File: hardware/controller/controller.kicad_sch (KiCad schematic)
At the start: 8 parts, among them SW1 RESET, U1 4050, U2 Pico, U3 Display_3.5", U4 4050, U5 Pico, U6 Display_3.5"

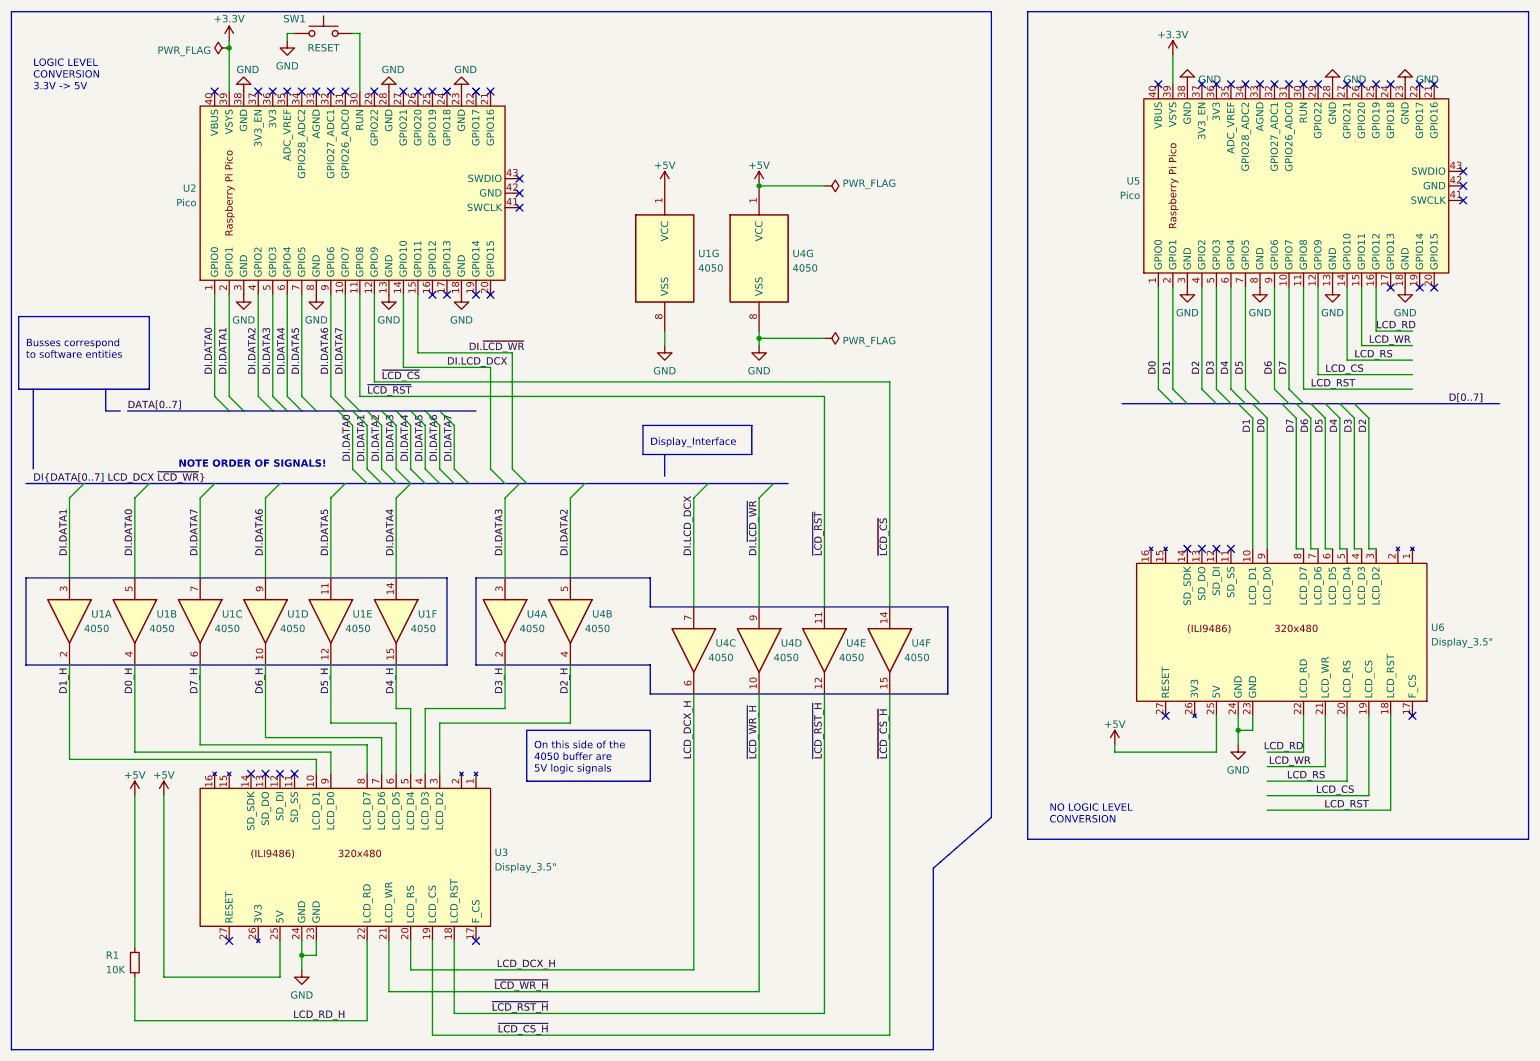
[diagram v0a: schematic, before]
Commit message: Removed 3.5 inch display from schematic
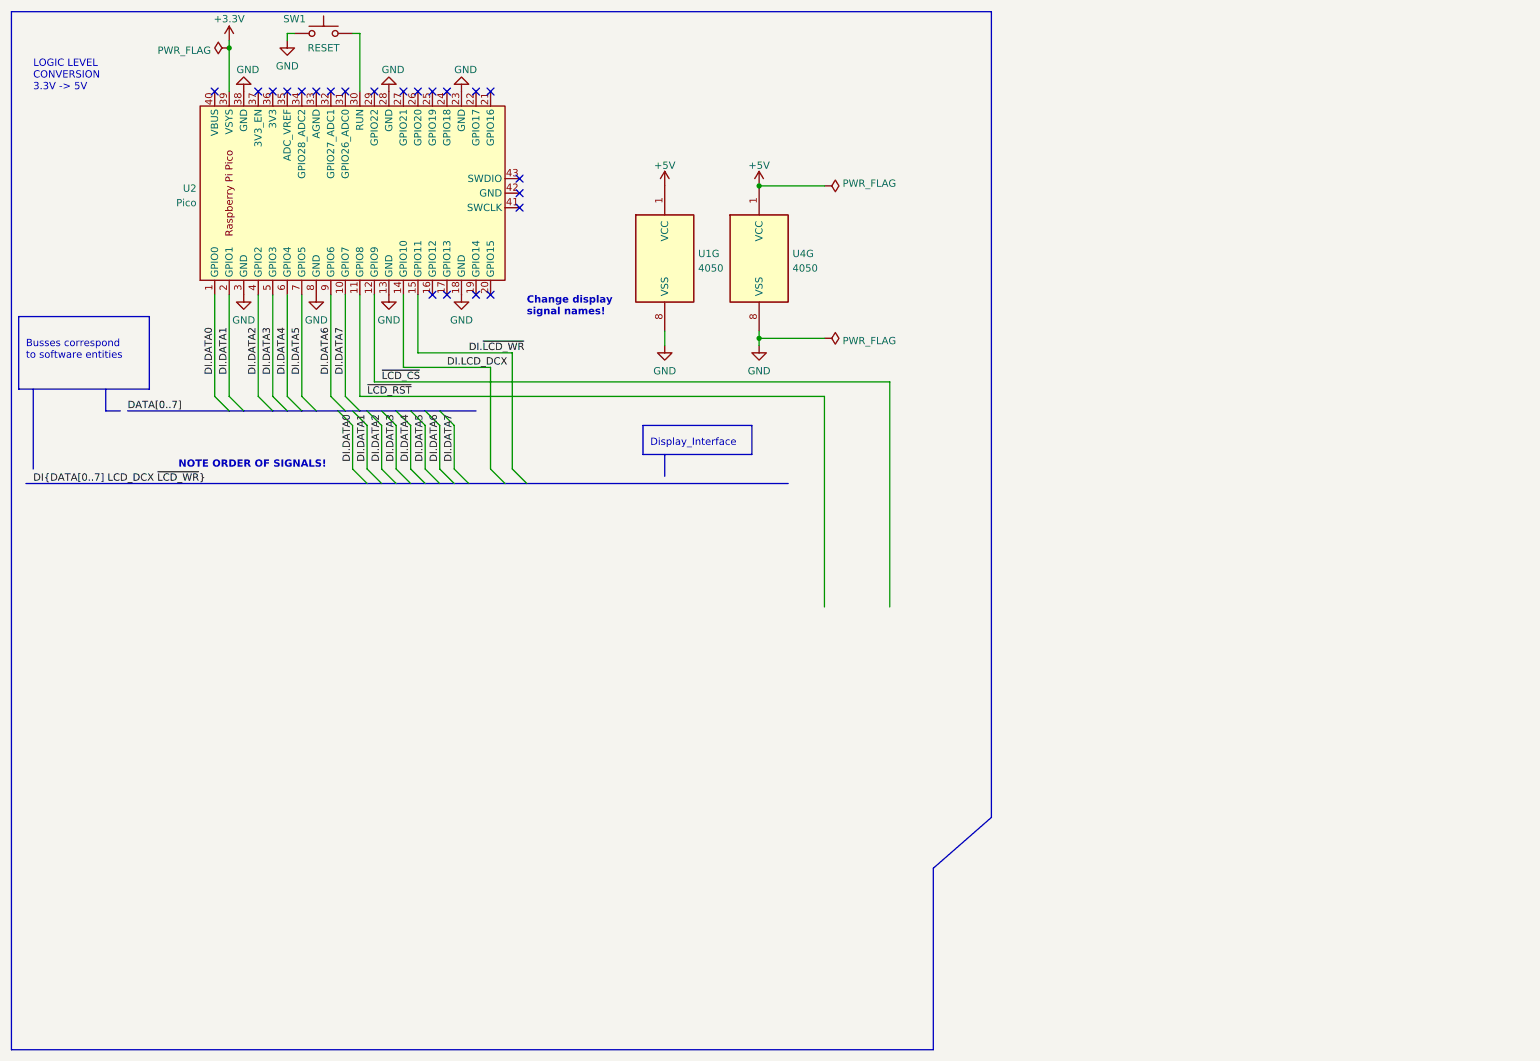
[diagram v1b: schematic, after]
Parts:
- removed R1: 10K, symbol Device:R_Small
- removed unit 1 of U1
- removed unit 2 of U1
- removed unit 3 of U1
- removed unit 5 of U1
- removed unit 4 of U1
- removed unit 6 of U1
- removed U3, U6: Display_3.5", symbol project:Display_3.5{dblquote}
- removed unit 4 of U4
- removed unit 1 of U4
- removed unit 6 of U4
- removed unit 3 of U4
- removed unit 5 of U4
- removed unit 2 of U4
- removed U5: Pico, RPi_Pico:RPi_Pico_SMD_TH, symbol MCU_RaspberryPi_and_Boards:Pico
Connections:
- no-connect marks 56 -> 22
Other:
- note added: "Change display signal names!"
- note removed: "NO LOGIC LEVEL CONVERSION"
- note removed: "On this side of the 4050 buffer are 5V logic signals"

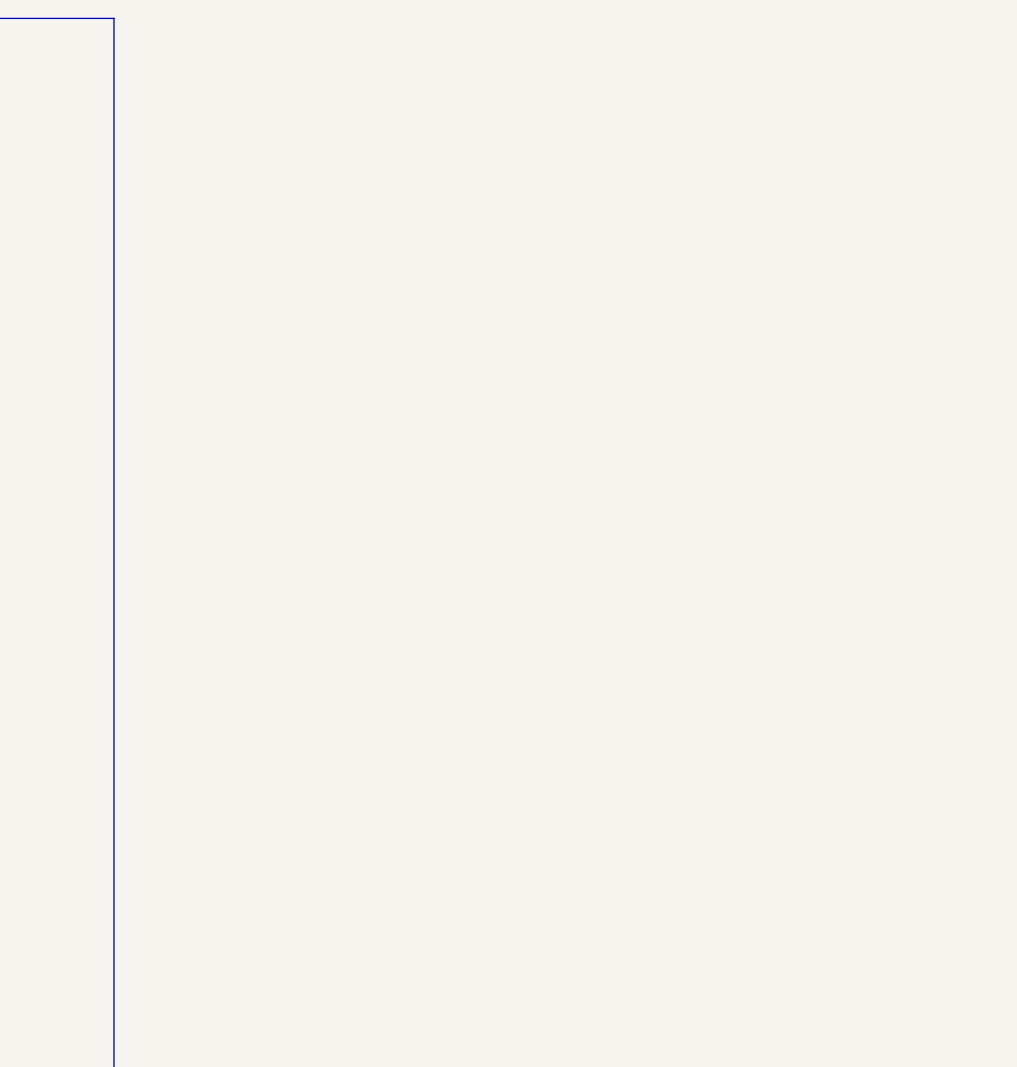
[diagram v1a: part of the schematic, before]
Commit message: Revised powerchain (diode, new symbol)
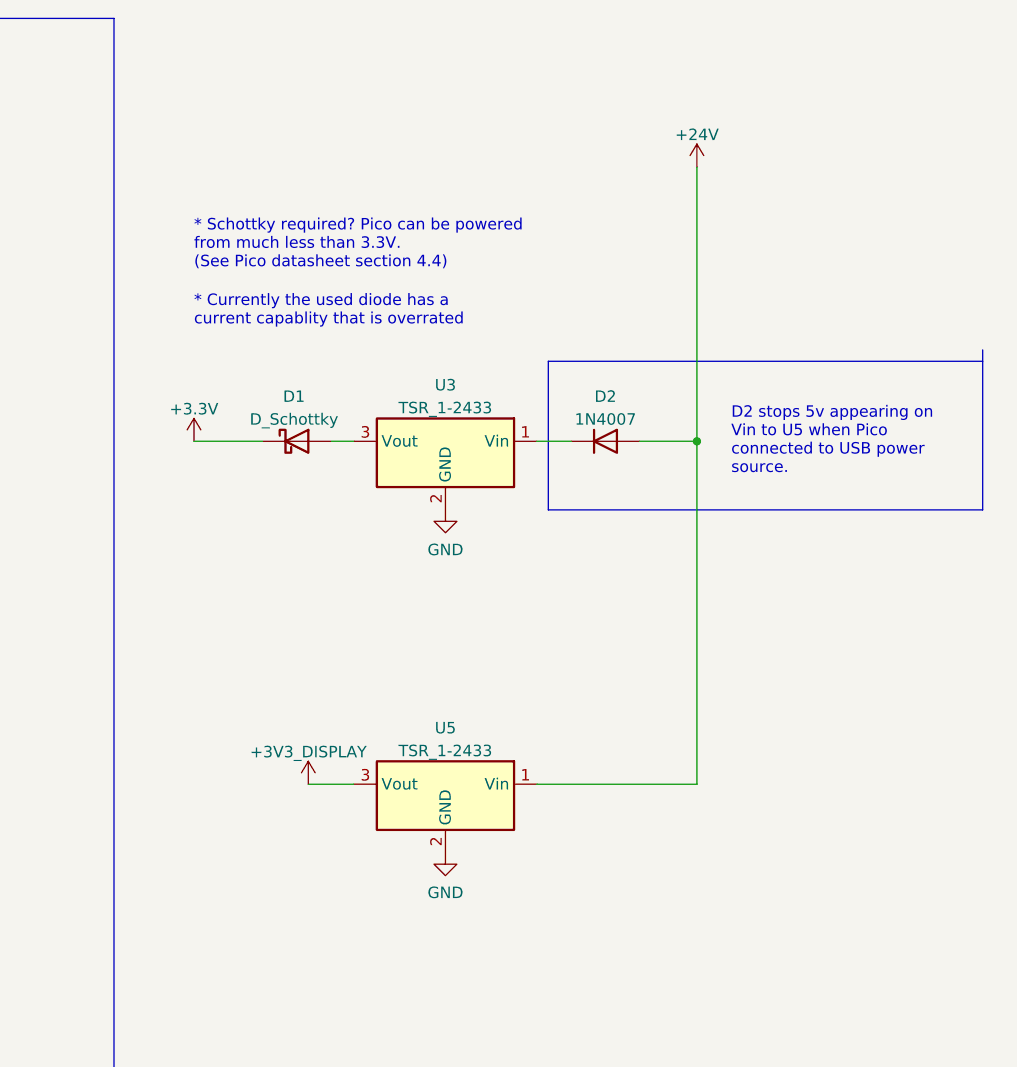
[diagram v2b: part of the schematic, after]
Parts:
- added D1: D_Schottky, symbol Device:D_Schottky
- added D2: 1N4007, Diode_THT:D_DO-41_SOD81_P10.16mm_Horizontal, symbol Diode:1N4007
- added U3, U5: TSR_1-2433, Converter_DCDC:Converter_DCDC_TRACO_TSR-1_THT, symbol Regulator_Switching:TSR_1-2433
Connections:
- net +3V3: now also D1.1 (K), U5.3 (Vout)
- net GND: now also U3.2 (GND), U5.2 (GND)
- new net: D2.1 (K), U3.1 (Vin)
- new net: D1.2 (A), U3.3 (Vout)
- new net +24V: D2.2 (A), U5.1 (Vin)
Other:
- note added: "* Currently the used diode has a current capablity that is overrated"
- note added: "* Schottky required? Pico can be powered from much less than 3.3V. (See Pico datasheet section 4.4)"
- note added: "D2 stops 5v appearing on Vin to U5 when Pico connected to USB power source."

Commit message: Added sense signal
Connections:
- net +3V3: now also U2.21 (GPIO16)
- no-connect marks 22 -> 21
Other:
- note added: "To GPIO16"
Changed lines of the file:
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@@
     (title "Modular-Amplifier - Controller")
+  )
+  (junction (at 209.55 100.33) (diameter 0) (color 0 0 0 0)
   )
   (junction (at 144.78 45.72) (diameter 0) (color 0 0 0 0)
@@
   (no_connect (at 95.25 64.77))
   (no_connect (at 97.79 64.77))
-  (no_connect (at 97.79 29.21))
   (no_connect (at 95.25 29.21))
   (no_connect (at 90.17 29.21))
@@
     (stroke (width 0) (type default) (color 0 0 0 0))
   )
+  (wire (pts (xy 209.55 100.33) (xy 212.09 100.33))
+    (stroke (width 0) (type default) (color 0 0 0 0))
+  )
   (bus (pts (xy 78.74 97.79) (xy 81.28 97.79))
     (stroke (width 0) (type default) (color 0 0 0 0))
@@
     (stroke (width 0) (type default) (color 0 0 0 0))
   )
+  (wire (pts (xy 195.58 106.68) (xy 209.55 106.68))
+    (stroke (width 0) (type default) (color 0 0 0 0))
+  )
+  (wire (pts (xy 97.79 29.21) (xy 97.79 21.59))
+    (stroke (width 0) (type default) (color 0 0 0 0))
+  )
   (polyline (pts (xy 124.46 87.63) (xy 124.46 92.71))
     (stroke (width 0) (type default) (color 0 0 0 0))
@@
     (stroke (width 0) (type default) (color 0 0 0 0))
   )
-  (polyline (pts (xy 281.94 52.07) (xy 281.94 69.85))
-    (stroke (width 0) (type default) (color 0 0 0 0))
-  )
   (wire (pts (xy 74.93 64.77) (xy 74.93 82.55))
     (stroke (width 0) (type default) (color 0 0 0 0))
@@
     (stroke (width 0) (type default) (color 0 0 0 0))
   )
+  (wire (pts (xy 97.79 21.59) (xy 111.76 21.59))
+    (stroke (width 0) (type default) (color 0 0 0 0))
+  )
   (wire (pts (xy 97.79 77.47) (xy 97.79 95.25))
     (stroke (width 0) (type default) (color 0 0 0 0))
@@
     (stroke (width 0) (type default) (color 0 0 0 0))
   )
-  (wire (pts (xy 207.01 100.33) (xy 212.09 100.33))
+  (wire (pts (xy 207.01 100.33) (xy 209.55 100.33))
     (stroke (width 0) (type default) (color 0 0 0 0))
   )
@@
   )
   (bus (pts (xy 81.28 85.09) (xy 83.82 85.09))
+    (stroke (width 0) (type default) (color 0 0 0 0))
+  )
+  (wire (pts (xy 209.55 100.33) (xy 209.55 106.68))
+    (stroke (width 0) (type default) (color 0 0 0 0))
+  )
+  (polyline (pts (xy 281.94 53.34) (xy 281.94 69.85))
     (stroke (width 0) (type default) (color 0 0 0 0))
   )
@@
     (effects (font (size 1.27 1.27) (thickness 0.254) bold) (justify left bottom))
   )
+  (text "To GPIO16" (at 196.85 110.49 0)
+    (effects (font (size 1.27 1.27)) (justify left bottom))
+  )
   (label "DI.DATA3" (at 59.69 78.74 90)
     (effects (font (size 1.27 1.27)) (justify left bottom))
@@
     (effects (font (size 1.27 1.27)) (justify left bottom))
   )
+  (label "SENSE" (at 104.14 21.59 0)
+    (effects (font (size 1.27 1.27)) (justify left bottom))
+  )
   (label "DI.DATA7" (at 72.39 78.74 90)
     (effects (font (size 1.27 1.27)) (justify left bottom))
@@
     (effects (font (size 1.27 1.27)) (justify left bottom))
   )
+  (label "SENSE" (at 196.85 106.68 0)
+    (effects (font (size 1.27 1.27)) (justify left bottom))
+  )

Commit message: Controller schematic and PCB design
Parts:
- removed U1, U4: 4050, symbol 4xxx:4050
- added H1, H2, H3, H4: MountingHole, MountingHole:MountingHole_3.2mm_M3, symbol Mechanical:MountingHole
- added J1: Conn_02x15_Odd_Even, Connector_PinSocket_2.54mm:PinSocket_2x15_P2.54mm_Vertical, symbol Connector_Generic:Conn_02x15_Odd_Even
- added J10: conn_wifi, Connector_JST:JST_PH_B8B-PH-K_1x08_P2.00mm_Vertical, symbol Connector_Generic:Conn_01x08
- added J11: conn_gpio, Connector_PinHeader_2.54mm:PinHeader_1x04_P2.54mm_Vertical, symbol Connector_Generic:Conn_01x04
- added J2, J3: Conn_01x20, Connector_PinSocket_2.54mm:PinSocket_1x20_P2.54mm_Vertical, symbol Connector_Generic:Conn_01x20
- added J4: Conn_01x02, Connector_JST:JST_XH_B2B-XH-A_1x02_P2.50mm_Vertical, symbol Connector_Generic:Conn_01x02
- added J5: conn_vol, Connector_JST:JST_PH_B5B-PH-K_1x05_P2.00mm_Vertical, symbol Connector_Generic:Conn_01x05
- added J6: conn_bl, Connector_JST:JST_PH_B5B-PH-K_1x05_P2.00mm_Vertical, symbol Connector_Generic:Conn_01x05
- added J7: conn_br, Connector_JST:JST_PH_B5B-PH-K_1x05_P2.00mm_Vertical, symbol Connector_Generic:Conn_01x05
- added J8: conn_dsp, Connector_JST:JST_PH_B4B-PH-K_1x04_P2.00mm_Vertical, symbol Connector_Generic:Conn_01x04
- added J9: conn_i2s_mplx, Connector_JST:JST_PH_B4B-PH-K_1x04_P2.00mm_Vertical, symbol Connector_Generic:Conn_01x04
- added R1: 10k, Resistor_SMD:R_0805_2012Metric_Pad1.20x1.40mm_HandSolder, symbol Device:R_Small
- added R2, R3: 2.2K, Resistor_SMD:R_0805_2012Metric_Pad1.20x1.40mm_HandSolder, symbol Device:R_Small
- added U1: Display_5"_RA8875, symbol project:Display_5{dblquote}_RA8875
- added U2: TSR_1-2433, Converter_DCDC:Converter_DCDC_TRACO_TSR-1_THT, symbol Regulator_Switching:TSR_1-2433
- D1: footprint (none) -> Diode_THT:D_DO-15_P12.70mm_Horizontal; Source (none) -> https://www.conrad.de/de/p/tru-components-schottky-diode-gl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; Uf (none) -> 500mV
- SW1: footprint (none) -> Button_Switch_THT:SW_PUSH_6mm_H4.3mm
- renumbered U2 to #U2
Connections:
- net +24V: now also J4.1 (Pin_1), U2.1 (Vin)
- net +3V3: now also J11.2 (Pin_2), J3.19 (Pin_19), J5.4 (Pin_4), J6.2 (Pin_2), J7.2 (Pin_2), J9.2 (Pin_2), R2.1, R3.1; no longer #U2.21 (GPIO16), U5.3 (Vout)
- net DI.DATA0: now also #U2.17 (GPIO13), J1.15 (Pin_15), J2.17 (Pin_17), U1.15 (DB0); no longer #U2.1 (GPIO0)
- net DI.DATA1: now also #U2.16 (GPIO12), J1.16 (Pin_16), J2.16 (Pin_16), U1.16 (DB1); no longer #U2.2 (GPIO1)
- net DI.DATA2: now also #U2.15 (GPIO11), J1.17 (Pin_17), J2.15 (Pin_15), U1.17 (DB2); no longer #U2.4 (GPIO2)
- net DI.DATA3: now also #U2.14 (GPIO10), J1.18 (Pin_18), J2.14 (Pin_14), U1.18 (DB3); no longer #U2.5 (GPIO3)
- net DI.DATA4: now also J1.19 (Pin_19), J3.6 (Pin_6), U1.19 (DB4); no longer #U2.6 (GPIO4)
- net DI.DATA5: now also #U2.27 (GPIO21), J1.20 (Pin_20), J3.7 (Pin_7), U1.20 (DB5); no longer #U2.7 (GPIO5)
- net DI.DATA6: now also #U2.29 (GPIO22), J1.21 (Pin_21), J3.9 (Pin_9), U1.21 (DB6); no longer #U2.9 (GPIO6)
- net DI.DATA7: now also #U2.31 (GPIO26_ADC0), J1.22 (Pin_22), J3.11 (Pin_11), U1.22 (DB7); no longer #U2.10 (GPIO7)
- net DI.LCD_DCX: now also #U2.32 (GPIO27_ADC1), J1.8 (Pin_8), J3.12 (Pin_12), U1.8 (RS); no longer #U2.14 (GPIO10)
- net DI.~{LCD_WR}: now also #U2.34 (GPIO28_ADC2), J1.6 (Pin_6), J3.14 (Pin_14), U1.6 (WR); no longer #U2.15 (GPIO11)
- net GND: now also J1.1 (Pin_1), J1.13 (Pin_13), J1.2 (Pin_2), J10.1 (Pin_1), J11.1 (Pin_1), J2.13 (Pin_13), J2.18 (Pin_18), J2.3 (Pin_3), J2.8 (Pin_8), J3.18 (Pin_18), J3.3 (Pin_3), J3.8 (Pin_8), J4.2 (Pin_2), J5.5 (Pin_5), J6.1 (Pin_1), J7.1 (Pin_1), J8.1 (Pin_1), J9.1 (Pin_1), U1.1 (GND), U1.13 (GND), U1.2 (GND), U2.2 (GND)
- net ~{LCD_CS}: now also #U2.20 (GPIO15), J1.7 (Pin_7), J2.20 (Pin_20), U1.7 (~{CS}); no longer #U2.12 (GPIO9)
- net ~{WIFI_RESET}: now reaches #U2.19 (GPIO14)
- net ~{WIFI_RESET}: now also J10.8 (Pin_8), J2.19 (Pin_19)
- net SPI0_CS: now reaches #U2.22 (GPIO17)
- net SPI0_CS: now also J10.6 (Pin_6), J3.2 (Pin_2)
- net SPI0_SCK: now reaches #U2.24 (GPIO18)
- net SPI0_SCK: now also J10.3 (Pin_3), J3.4 (Pin_4)
- net SPI0_TX: now reaches #U2.25 (GPIO19)
- net SPI0_TX: now also J10.5 (Pin_5), J3.5 (Pin_5)
- net DATA4: now reaches #U2.26 (GPIO20)
- net MCU_RESET: now reaches #U2.30 (RUN), SW1.2
- net MCU_RESET: now also J3.10 (Pin_10)
- net ~{LCD_RST} renamed VOL_C
- net VOL_C: now also J2.11 (Pin_11), J5.3 (Pin_3)
- new net +3V3_AUX: J10.2 (Pin_2), J8.2 (Pin_2), U2.3 (Vout)
- new net +3V3_DISPLAY: J1.3 (Pin_3), J1.4 (Pin_4), R1.1, U1.3 (PWR), U1.4 (PWR), U5.3 (Vout)
- new net GPIO0: #U2.1 (GPIO0), J11.3 (Pin_3), J2.1 (Pin_1)
- new net GPIO9: #U2.12 (GPIO9), J11.4 (Pin_4), J2.12 (Pin_12)
- new net I2C0_SCL: #U2.7 (GPIO5), J2.7 (Pin_7), J6.4 (Pin_4), J7.4 (Pin_4), J8.4 (Pin_4), J9.4 (Pin_4), R2.2
- new net I2C0_SDA: #U2.6 (GPIO4), J2.6 (Pin_6), J6.3 (Pin_3), J7.3 (Pin_3), J8.3 (Pin_3), J9.3 (Pin_3), R3.2
- new net INT_BL: #U2.2 (GPIO1), J2.2 (Pin_2), J6.5 (Pin_5)
- new net INT_BR: #U2.4 (GPIO2), J2.4 (Pin_4), J7.5 (Pin_5)
- new net LCD_READ: J1.5 (Pin_5), R1.2, U1.5 (RD)
- new net SPI0_RX: #U2.21 (GPIO16), J10.4 (Pin_4), J3.1 (Pin_1)
- new net VOL_A: #U2.9 (GPIO6), J2.9 (Pin_9), J5.1 (Pin_1)
- new net VOL_B: #U2.10 (GPIO7), J2.10 (Pin_10), J5.2 (Pin_2)
- new net WIFI_BUSY: #U2.5 (GPIO3), J10.7 (Pin_7), J2.5 (Pin_5)
- no-connect marks 21 -> 37
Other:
- note added: "Buttons Left"
- note added: "Buttons Right"
- note added: "CHECK that the display pins can all be put into the correct mode"
- note added: "CONNECTORS"
- note added: "Careful with Teensy 4.1 power up sequence. See https://forum.pjrc.com/threads/64468-Teensy40-only-3-3V-power-supply?p=259469%26viewfull=1#post259469"
- note added: "DI = Display_Interface"
- note added: "DISPLAY CONNECTOR"
- note added: "DSP"
- note added: "EXTERNAL DISPLAY BOARD"
- note added: "GPIO"
- note added: "I2S Multiplexer"
- note added: "Only 8 bit bus used"
- note added: "Open Source Hardware"
- note added: "PICO MCU"
- note added: "POWER"
- note added: "Use JST XH connector as need connector that can handle up to 3A."
- note added: "Use Pin Header"
- note added: "Vol_[A..C] need to be on consecutive GPIO pins so that a PIO can be used if required."
- note added: "Volume"
- note added: "WIFI"
- note removed: "Busses correspond to software entities"
- note removed: "Change display signal names!"
- note removed: "Display_Interface"
- note removed: "LOGIC LEVEL CONVERSION 3.3V -> 5V"
- note removed: "NOTE ORDER OF SIGNALS!"
- note removed: "To GPIO16"
- moved on the sheet: SW1
